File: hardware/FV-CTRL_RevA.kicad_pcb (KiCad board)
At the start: 2 copper layers, 100 x 100 mm, 73 parts, among them J1 12V_IN, J10 IR_RX2, J11 IR_TX1 (Col 1), J12 IR_TX2 (Col 2), J13 LS1 (DNP), J14 LS2 (DNP), J15 LS3 (DNP), J16 LS4 (DNP), J17 I2C_RESERVED, J18 ESP32_Left (Pins 1-19), J19 ESP32_Right (Pins 20-38), J2 XH-M401 (6.0V 8A), J3 AUX_BUCK (DNP), J4 MP1584EN (5V Logic), J5 S1_TOP, J6 S1_BOT, J7 S2_TOP, J8 S2_BOT, J9 IR_RX1, Q1 IRF9540N, Q2 S8050

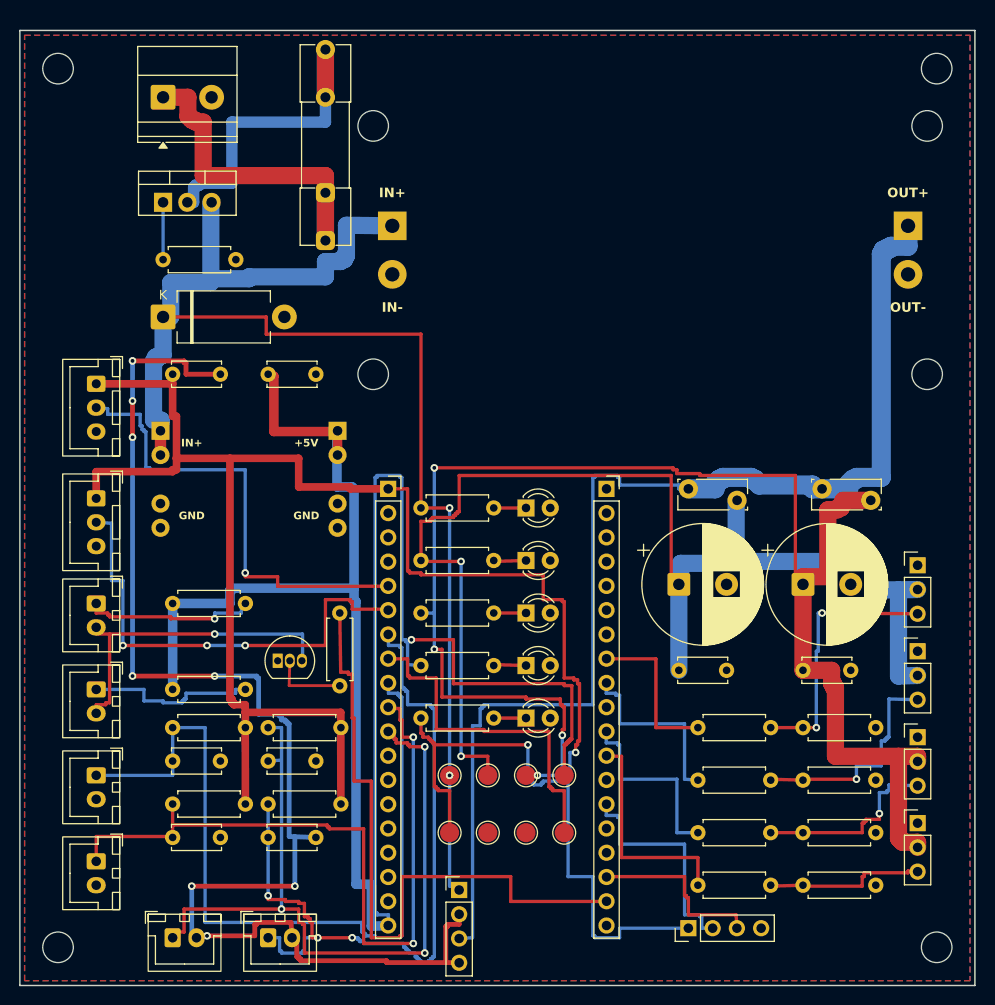
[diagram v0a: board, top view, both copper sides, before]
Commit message: feat(pcb): implement zero-DRC layout with vector segment obstacles, via clearance grid, and 100% net routing
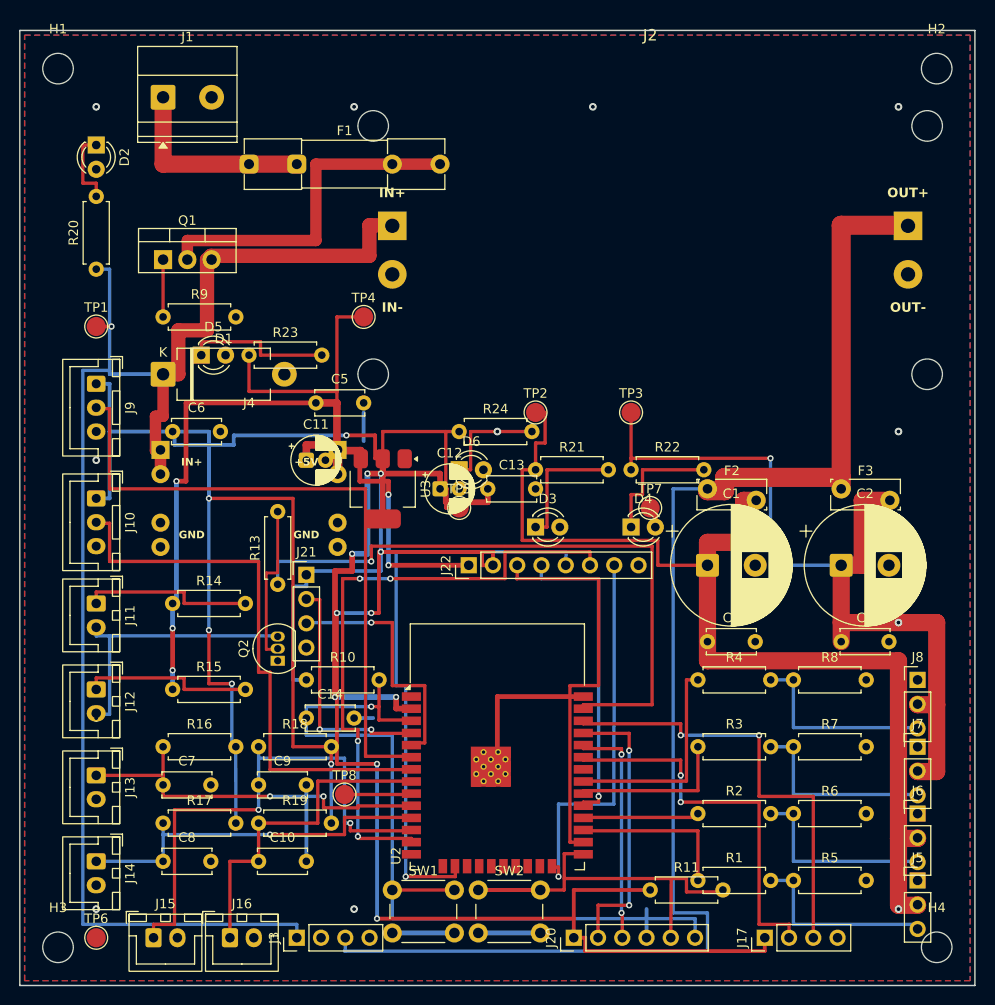
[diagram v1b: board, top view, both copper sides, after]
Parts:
- removed J18: ESP32_Left (Pins 1-19), PinSocket_1x19_P2.54mm_Vertical
- removed J19: ESP32_Right (Pins 20-38), PinSocket_1x19_P2.54mm_Vertical
- added C11: 10uF 16V, CP_Radial_D5.0mm_P2.00mm, F.Cu at (130.0, 145.0)
- added C12: 22uF 16V, CP_Radial_D5.0mm_P2.00mm, F.Cu at (144.0, 148.0)
- added C13: 100nF, C_Disc_D5.0mm_W2.5mm_P5.00mm, F.Cu at (149.0, 148.0)
- added C14: 100nF, C_Disc_D5.0mm_W2.5mm_P5.00mm, F.Cu at (130.0, 172.0)
- added J20: PROG_UART0, PinHeader_1x06_P2.54mm_Vertical, F.Cu at (158.0, 195.0)
- added J21: SENSOR_ADC, PinHeader_1x04_P2.54mm_Vertical, F.Cu at (130.0, 157.0)
- added J22: SENSOR_DIGITAL, PinHeader_1x08_P2.54mm_Vertical, F.Cu at (147.0, 156.0)
- added R10: 10k, R_Axial_DIN0207_L6.3mm_D2.5mm_P7.62mm_Horizontal, F.Cu at (130.0, 168.0)
- added R11: 10k, R_Axial_DIN0207_L6.3mm_D2.5mm_P7.62mm_Horizontal, F.Cu at (166.0, 190.0)
- added SW1: SW_EN, SW_PUSH_6mm_H5mm, F.Cu at (139.0, 190.0)
- added SW2: SW_BOOT, SW_PUSH_6mm_H5mm, F.Cu at (148.0, 190.0)
- added U2: ESP32-WROOM-32, ESP32-WROOM-32_HandSolder, F.Cu at (150.0, 178.0)
- added U3: AMS1117-3.3, SOT-223-3_TabPin2, F.Cu at (138.0, 148.0)
- moved TP1 59.8 mm to (108.0, 131.0)
- moved D2 58.9 mm to (108.0, 112.0), turned to -90 degrees
- moved TP4 52.4 mm to (136.0, 130.0)
- moved D5 47.0 mm to (119.0, 134.0)
- moved TP6 42.4 mm to (108.0, 195.0)
- moved R20 42.2 mm to (108.0, 125.0), turned to 90 degrees
- moved TP3 39.6 mm to (164.0, 140.0)
- moved TP2 38.3 mm to (154.0, 140.0)
- moved R23 37.2 mm to (124.0, 134.0)
- moved TP7 36.4 mm to (166.0, 150.0)
- moved TP5 34.0 mm to (146.0, 150.0)
- moved J5 33.0 mm to (194.0, 189.0)
- moved R24 30.3 mm to (146.0, 142.0)
- moved D6 26.9 mm to (146.0, 146.0)
- moved R22 26.6 mm to (164.0, 146.0)
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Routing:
- net +3V3: track 228.0 -> 398.6 mm, vias 2 -> 15
- net GND: track 141.1 -> 46.2 mm
- net +5V: track 208.1 -> 115.3 mm, vias 1 -> 5
- net ESP_EN: track 0.00 -> 86.6 mm, vias 0 -> 1
- net +6V_B: track 159.9 -> 88.7 mm, vias 4 -> 2
- net EXP_IO14: track 0.00 -> 64.9 mm, vias 0 -> 4
- net EXP_IO13: track 0.00 -> 60.4 mm, vias 0 -> 1
- net LS1: track 87.1 -> 39.6 mm, vias 0 -> 2
- net LS4: track 81.7 -> 35.4 mm, vias 3 -> 0
- net ESP_IO0: track 0.00 -> 45.7 mm
- net EXP_IO4: track 0.00 -> 42.1 mm
- net LS2: track 79.1 -> 38.8 mm, vias 2 -> 1
- net EXP_IO2: track 0.00 -> 40.0 mm, vias 0 -> 1
- net EXP_IO5: track 0.00 -> 32.8 mm, vias 0 -> 1
- net SPARE_GPIO33: track 36.6 -> 7.00 mm
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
